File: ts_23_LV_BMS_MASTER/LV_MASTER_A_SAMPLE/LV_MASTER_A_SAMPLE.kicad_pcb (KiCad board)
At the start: 4 copper layers, 77.5 x 46.9 mm, 117 parts, among them J1 DT 12P, J2 UART, J3 BOOT1, J4 STLINK, J5 Conn_01x02_Male, J6 Conn_02x02_Counter_Clockwise, J7 Conn_02x02_Counter_Clockwise, Q1 STD7NK40Z, Q2 STD7NK40Z, T1 HX1188NL, U1 STM32F446RET7, U2 TLV70033_SOT23-5, U4 ADM3053, U5 B82786C0104H002, U6 LTC6820, U7 ISO1540, U8 ADS1115, U9 ADUM3221, Y1 ECS-80-18-30-JGN-TR, Y2 FC-135_32.7680KA-A5

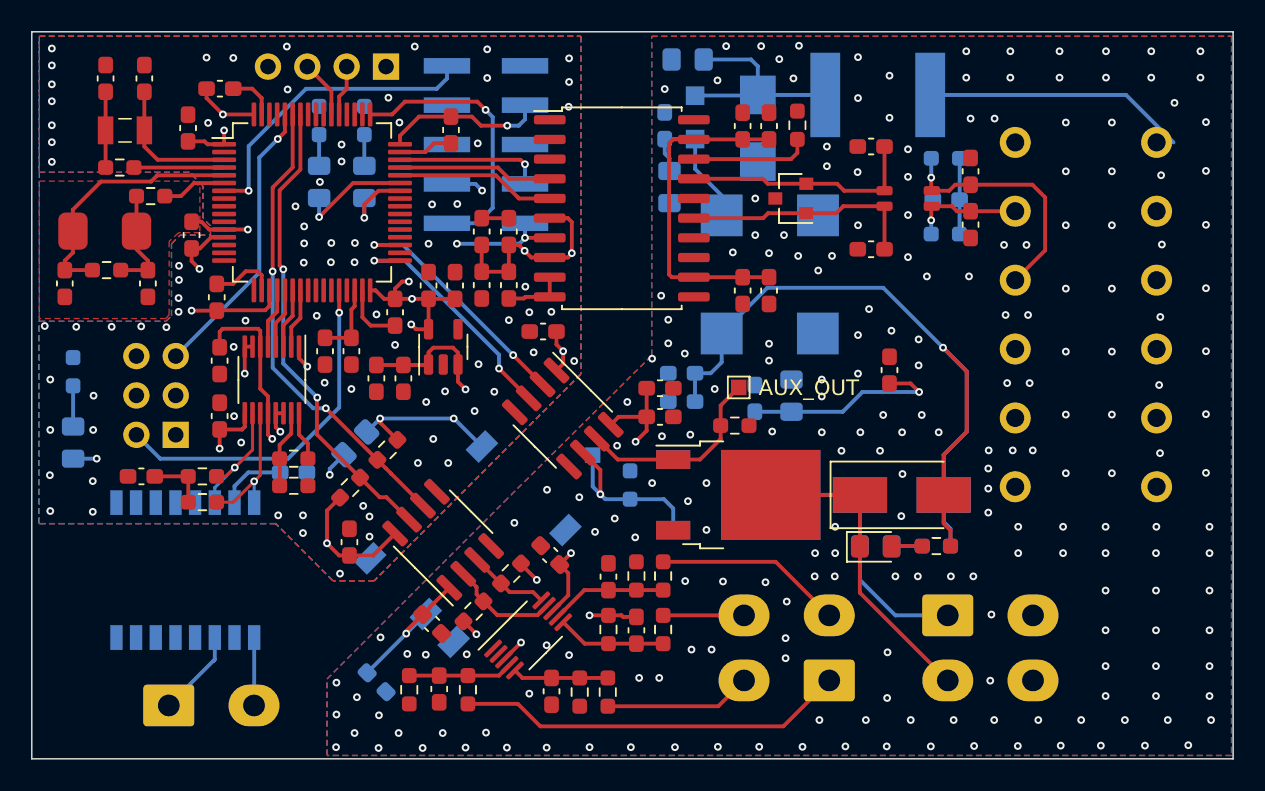
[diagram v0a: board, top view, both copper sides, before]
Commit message: resolved diff. pair routing issues on master module
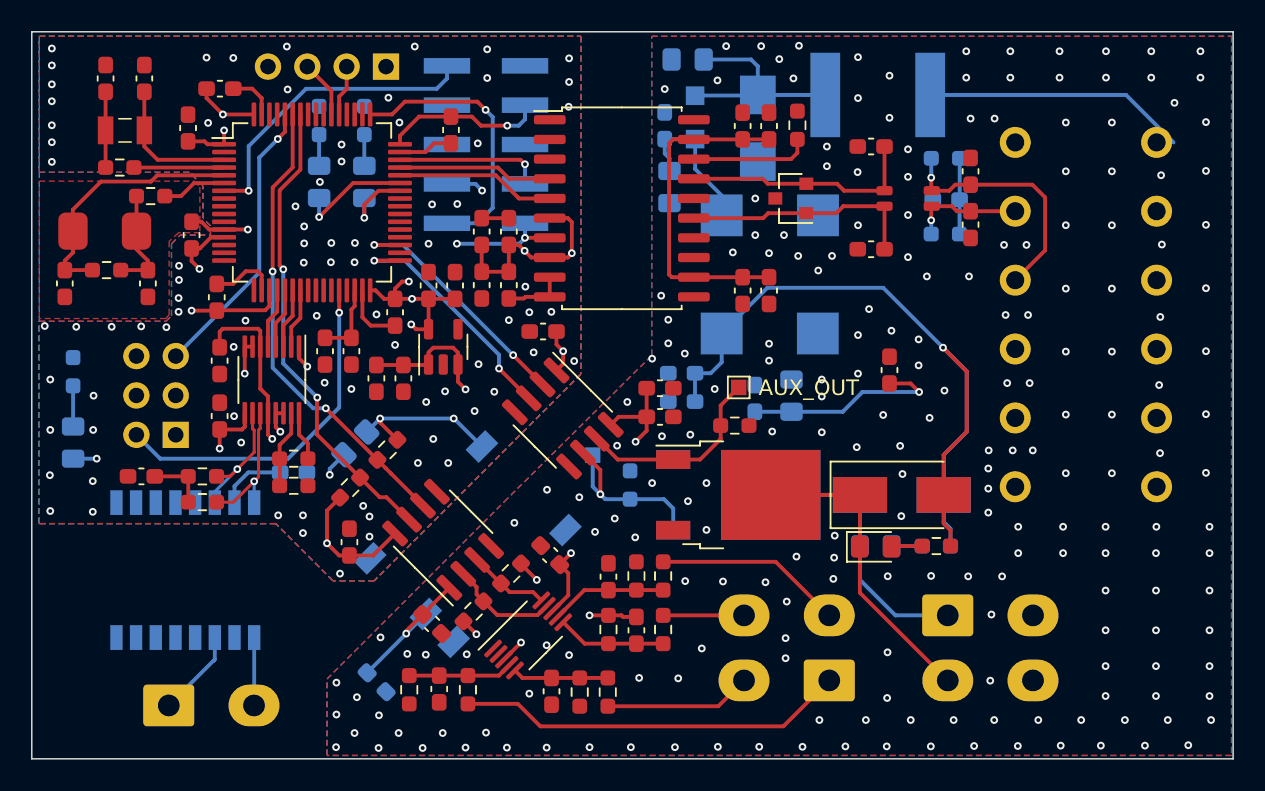
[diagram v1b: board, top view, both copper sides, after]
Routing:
- net GND: vias 216 -> 212
